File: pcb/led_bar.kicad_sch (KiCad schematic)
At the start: 18 parts

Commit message: Parts
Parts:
- D10: renamed from D30; LCSC (none) -> C22371521
- D11: renamed from D31; LCSC (none) -> C22371521
- D12: renamed from D32; LCSC (none) -> C22371521
- D13: renamed from D33; LCSC (none) -> C22371521
- D14: renamed from D34; LCSC (none) -> C22371521
- D15: renamed from D35; LCSC (none) -> C22371521
- D16: renamed from D36; LCSC (none) -> C22371521
- D17: renamed from D37; LCSC (none) -> C22371521
- D3: renamed from D26; LCSC (none) -> C22371521
- D4: renamed from D27; LCSC (none) -> C22371521
- D8: renamed from D28; LCSC (none) -> C22371521
- D9: renamed from D29; LCSC (none) -> C22371521
- renumbered C43 to C1, C44 to C2, C46 to C20, C47 to C21, C48 to C22, C45 to C3
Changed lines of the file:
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@@
 		(dnp no)
 		(fields_autoplaced yes)
-		(property "Reference" "#PWR0123"
+		(property "Reference" "#PWR0110"
 			(at 134.62 121.92 0)
 			(effects
@@
 		(on_board yes)
 		(dnp no)
-		(property "Reference" "D33"
+		(property "Reference" "D13"
 			(at 177.8 82.55 0)
 			(effects
@@
 			)
 		)
+		(property "LCSC" "C22371521"
+			(at 172.72 88.9 0)
+			(effects
+				(font
+					(size 1.27 1.27)
+				)
+				(hide yes)
+			)
+		)
 		(pin "1"
 		)
@@
 		(on_board yes)
 		(dnp no)
-		(property "Reference" "D29"
+		(property "Reference" "D9"
 			(at 116.84 82.55 0)
 			(effects
@@
 			)
 		)
+		(property "LCSC" "C22371521"
+			(at 111.76 88.9 0)
+			(effects
+				(font
+					(size 1.27 1.27)
+				)
+				(hide yes)
+			)
+		)
 		(pin "1"
 		)
@@
 		(on_board yes)
 		(dnp no)
-		(property "Reference" "D26"
+		(property "Reference" "D3"
 			(at 71.12 82.55 0)
 			(effects
@@
 			)
 		)
+		(property "LCSC" "C22371521"
+			(at 66.04 88.9 0)
+			(effects
+				(font
+					(size 1.27 1.27)
+				)
+				(hide yes)
+			)
+		)
 		(pin "1"
 		)
@@
 		(on_board yes)
 		(dnp no)
-		(property "Reference" "D30"
+		(property "Reference" "D10"
 			(at 132.08 82.55 0)
 			(effects
@@
 		)
 		(property "Description" ""
+			(at 127 88.9 0)
+			(effects
+				(font
+					(size 1.27 1.27)
+				)
+				(hide yes)
+			)
+		)
+		(property "LCSC" "C22371521"
 			(at 127 88.9 0)
 			(effects
@@
 		(on_board yes)
 		(dnp no)
-		(property "Reference" "#PWR0126"
+		(property "Reference" "#PWR0113"
 			(at 238.76 85.09 0)
 			(effects
@@
 		(on_board yes)
 		(dnp no)
-		(property "Reference" "D28"
+		(property "Reference" "D8"
 			(at 101.6 82.55 0)
 			(effects
@@
 			)
 		)
+		(property "LCSC" "C22371521"
+			(at 96.52 88.9 0)
+			(effects
+				(font
+					(size 1.27 1.27)
+				)
+				(hide yes)
+			)
+		)
 		(pin "1"
 		)
@@
 		(on_board yes)
 		(dnp no)
-		(property "Reference" "D31"
+		(property "Reference" "D11"
 			(at 147.32 82.55 0)
 			(effects
@@
 			)
 		)
+		(property "LCSC" "C22371521"
+			(at 142.24 88.9 0)
+			(effects
+				(font
+					(size 1.27 1.27)
+				)
+				(hide yes)
+			)
+		)
 		(pin "1"
 		)
@@
 		(on_board yes)
 		(dnp no)
-		(property "Reference" "C44"
+		(property "Reference" "C2"
 			(at 145.8468 111.8616 0)
 			(effects
@@
 		(dnp no)
 		(fields_autoplaced yes)
-		(property "Reference" "#PWR0124"
+		(property "Reference" "#PWR0111"
 			(at 134.62 114.3 0)
 			(effects
@@
 		(on_board yes)
 		(dnp no)
-		(property "Reference" "C47"
+		(property "Reference" "C21"
 			(at 164.8968 111.8616 0)
 			(effects
@@
 		(on_board yes)
 		(dnp no)
-		(property "Reference" "C46"
+		(property "Reference" "C20"
 			(at 158.5468 111.8616 0)
 			(effects
@@
 		(on_board yes)
 		(dnp no)
-		(property "Reference" "D35"
+		(property "Reference" "D15"
 			(at 208.28 82.55 0)
 			(effects
@@
 			)
 		)
+		(property "LCSC" "C22371521"
+			(at 203.2 88.9 0)
+			(effects
+				(font
+					(size 1.27 1.27)
+				)
+				(hide yes)
+			)
+		)
 		(pin "1"
 		)
@@
 		(on_board yes)
 		(dnp no)
-		(property "Reference" "C43"
+		(property "Reference" "C1"
 			(at 136.9568 111.8616 0)
 			(effects
@@
 		(on_board yes)
 		(dnp no)
-		(property "Reference" "D36"
+		(property "Reference" "D16"
 			(at 223.52 82.55 0)
 			(effects
@@
 			)
 		)
+		(property "LCSC" "C22371521"
+			(at 218.44 88.9 0)
+			(effects
+				(font
+					(size 1.27 1.27)
+				)
+				(hide yes)
+			)
+		)
 		(pin "1"
 		)
@@
 		(dnp no)
 		(fields_autoplaced yes)
-		(property "Reference" "#PWR0125"
+		(property "Reference" "#PWR0112"
 			(at 66.04 85.09 0)
 			(effects
@@
 		(on_board yes)
 		(dnp no)
-		(property "Reference" "C48"
+		(property "Reference" "C22"
 			(at 171.2468 111.8616 0)
 			(effects
@@
 		(on_board yes)
 		(dnp no)
-		(property "Reference" "D27"
+		(property "Reference" "D4"
 			(at 86.36 82.55 0)
 			(effects
@@
 			)
 		)
+		(property "LCSC" "C22371521"
+			(at 81.28 88.9 0)
+			(effects
+				(font
+					(size 1.27 1.27)
+				)
+				(hide yes)
+			)
+		)
 		(pin "1"
 		)
@@
 		(on_board yes)
 		(dnp no)
-		(property "Reference" "D32"
+		(property "Reference" "D12"
 			(at 162.56 82.55 0)
 			(effects
@@
 			)
 		)
+		(property "LCSC" "C22371521"
+			(at 157.48 88.9 0)
+			(effects
+				(font
+					(size 1.27 1.27)
+				)
+				(hide yes)
+			)
+		)
 		(pin "1"
 		)
@@
 		(on_board yes)
 		(dnp no)
-		(property "Reference" "D34"
+		(property "Reference" "D14"
 			(at 193.04 82.55 0)
 			(effects
@@
 			)
 		)
+		(property "LCSC" "C22371521"
+			(at 187.96 88.9 0)
+			(effects
+				(font
+					(size 1.27 1.27)
+				)
+				(hide yes)
+			)
+		)
 		(pin "1"
 		)
@@
 		(on_board yes)
 		(dnp no)
-		(property "Reference" "D37"
+		(property "Reference" "D17"
 			(at 238.76 82.55 0)
 			(effects
@@
 		)
 		(property "Description" ""
+			(at 233.68 88.9 0)
+			(effects
+				(font
+					(size 1.27 1.27)
+				)
+				(hide yes)
+			)
+		)
+		(property "LCSC" "C22371521"
 			(at 233.68 88.9 0)
 			(effects
@@
 		(dnp no)
 		(fields_autoplaced yes)
-		(property "Reference" "#PWR0127"
+		(property "Reference" "#PWR0114"
 			(at 233.68 104.14 0)
 			(effects
@@
 		(on_board yes)
 		(dnp no)
-		(property "Reference" "C45"
+		(property "Reference" "C3"
 			(at 152.1968 111.8616 0)
 			(effects

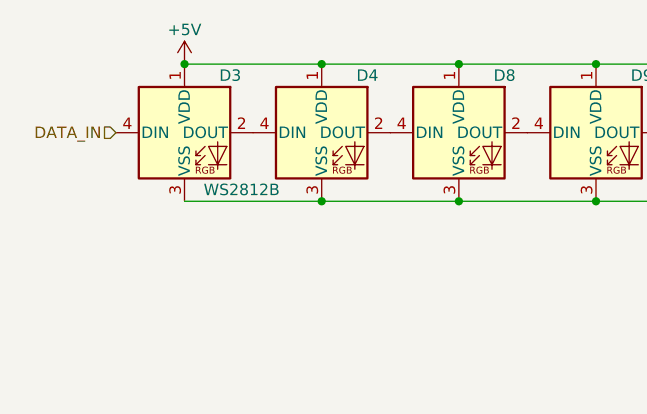
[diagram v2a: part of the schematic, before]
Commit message: LED Footprints fixed
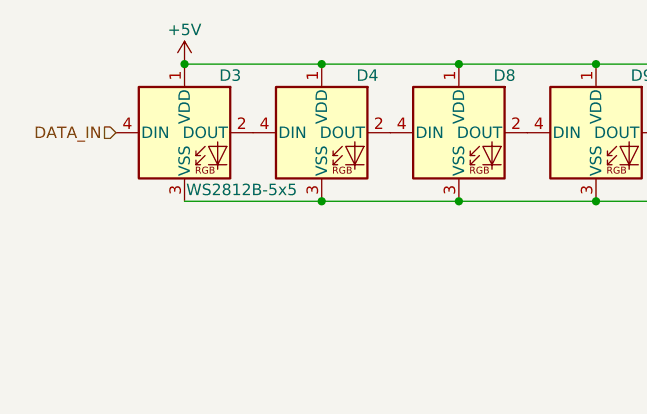
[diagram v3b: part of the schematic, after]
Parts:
- D10, D11, D12, D13, D14, D15, D16, D17, D3, D4, D8, D9: value WS2812B -> WS2812B-5x5
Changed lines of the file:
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@@
 			)
 		)
-		(property "Value" "WS2812B"
+		(property "Value" "WS2812B-5x5"
 			(at 184.15 87.1093 0)
 			(effects
@@
 			)
 		)
-		(property "Value" "WS2812B"
+		(property "Value" "WS2812B-5x5"
 			(at 123.19 87.1093 0)
 			(effects
@@
 			)
 		)
-		(property "Value" "WS2812B"
+		(property "Value" "WS2812B-5x5"
 			(at 72.39 95.25 0)
 			(effects
@@
 			)
 		)
-		(property "Value" "WS2812B"
+		(property "Value" "WS2812B-5x5"
 			(at 138.43 87.1093 0)
 			(effects
@@
 			)
 		)
-		(property "Value" "WS2812B"
+		(property "Value" "WS2812B-5x5"
 			(at 107.95 87.1093 0)
 			(effects
@@
 			)
 		)
-		(property "Value" "WS2812B"
+		(property "Value" "WS2812B-5x5"
 			(at 153.67 87.1093 0)
 			(effects
@@
 			)
 		)
-		(property "Value" "WS2812B"
+		(property "Value" "WS2812B-5x5"
 			(at 214.63 87.1093 0)
 			(effects
@@
 			)
 		)
-		(property "Value" "WS2812B"
+		(property "Value" "WS2812B-5x5"
 			(at 229.87 87.1093 0)
 			(effects
@@
 			)
 		)
-		(property "Value" "WS2812B"
+		(property "Value" "WS2812B-5x5"
 			(at 92.71 87.1093 0)
 			(effects
@@
 			)
 		)
-		(property "Value" "WS2812B"
+		(property "Value" "WS2812B-5x5"
 			(at 168.91 87.1093 0)
 			(effects
@@
 			)
 		)
-		(property "Value" "WS2812B"
+		(property "Value" "WS2812B-5x5"
 			(at 194.31 95.25 0)
 			(effects
@@
 			)
 		)
-		(property "Value" "WS2812B"
+		(property "Value" "WS2812B-5x5"
 			(at 245.11 87.1093 0)
 			(effects
